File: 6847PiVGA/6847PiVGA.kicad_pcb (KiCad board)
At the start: 2 copper layers, 66.3 x 57.7 mm, 51 parts, among them J1 DB15_Female_HighDensity, J2 Conn_01x06_Male, U1 MC6847, U2 AD724JRZ, U3 Pico, U4 AD813, U5 TXS0108EPW, U6 TXS0108EPW, U7 TXS0108EPW, Y1 4.433620MHz

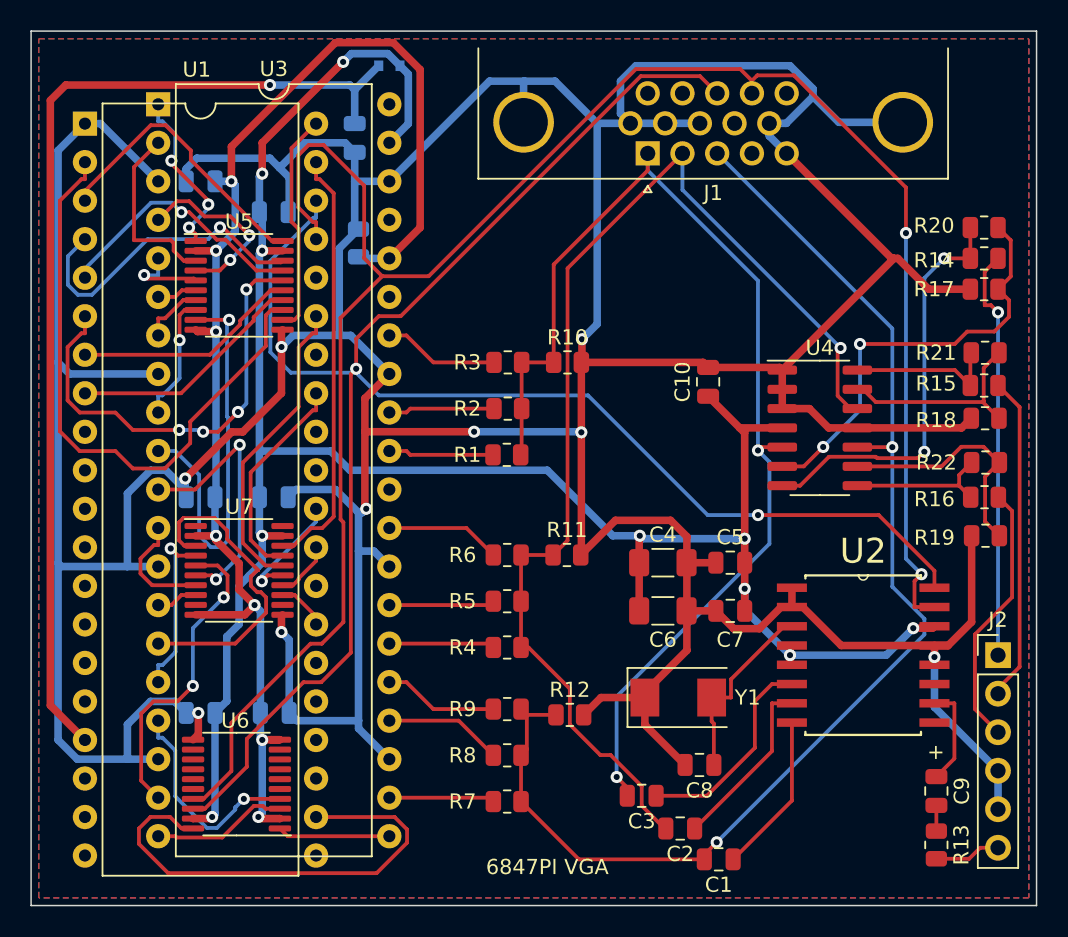
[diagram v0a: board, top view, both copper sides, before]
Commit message: fix voltage level to rgb sync signals
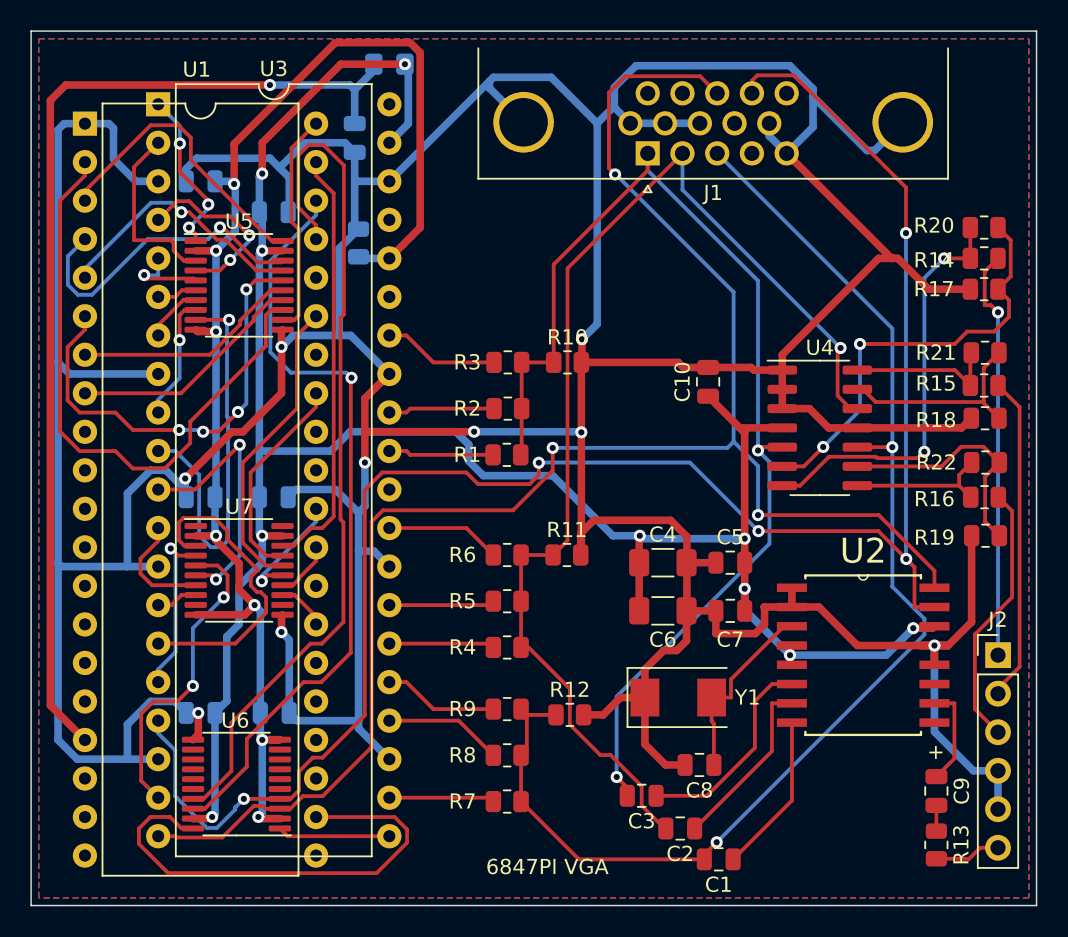
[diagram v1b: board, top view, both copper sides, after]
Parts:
- D1: footprint Diode_SMD:D_SOD-523 -> Diode_SMD:D_0805_2012Metric_Pad1.15x1.40mm_HandSolder
- moved D1 0.10 mm to (103.4, 83.2)
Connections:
- J1 pad 13: Hsync -> HsyncL
- J1 pad 14: Vsync -> VsyncL
- U2 pad 15: Vsync -> VsyncL
- U2 pad 16: Hsync -> HsyncL
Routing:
- net VsyncL: track 14.3 -> 121.2 mm, vias 1 -> 5
- net HsyncL: track 9.00 -> 112.9 mm, vias 0 -> 3
- net Hsync: track 130.5 -> 51.2 mm, vias 2 -> 1
- net Vsync: track 133.1 -> 56.7 mm, vias 2 -> 0
- net GND: track 419.1 -> 430.3 mm
- net +5VD: track 142.4 -> 143.8 mm
- net OE: track 90.1 -> 90.9 mm
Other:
- board text added: "6847PI VGA Revision 4"
- board text removed: "6847PI VGA Revision 3"
